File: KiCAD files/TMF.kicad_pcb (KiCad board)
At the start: 2 copper layers, 100 x 103 mm, 90 parts, among them J1 Conn_01x04_Pin, J2 Conn_01x04_Pin

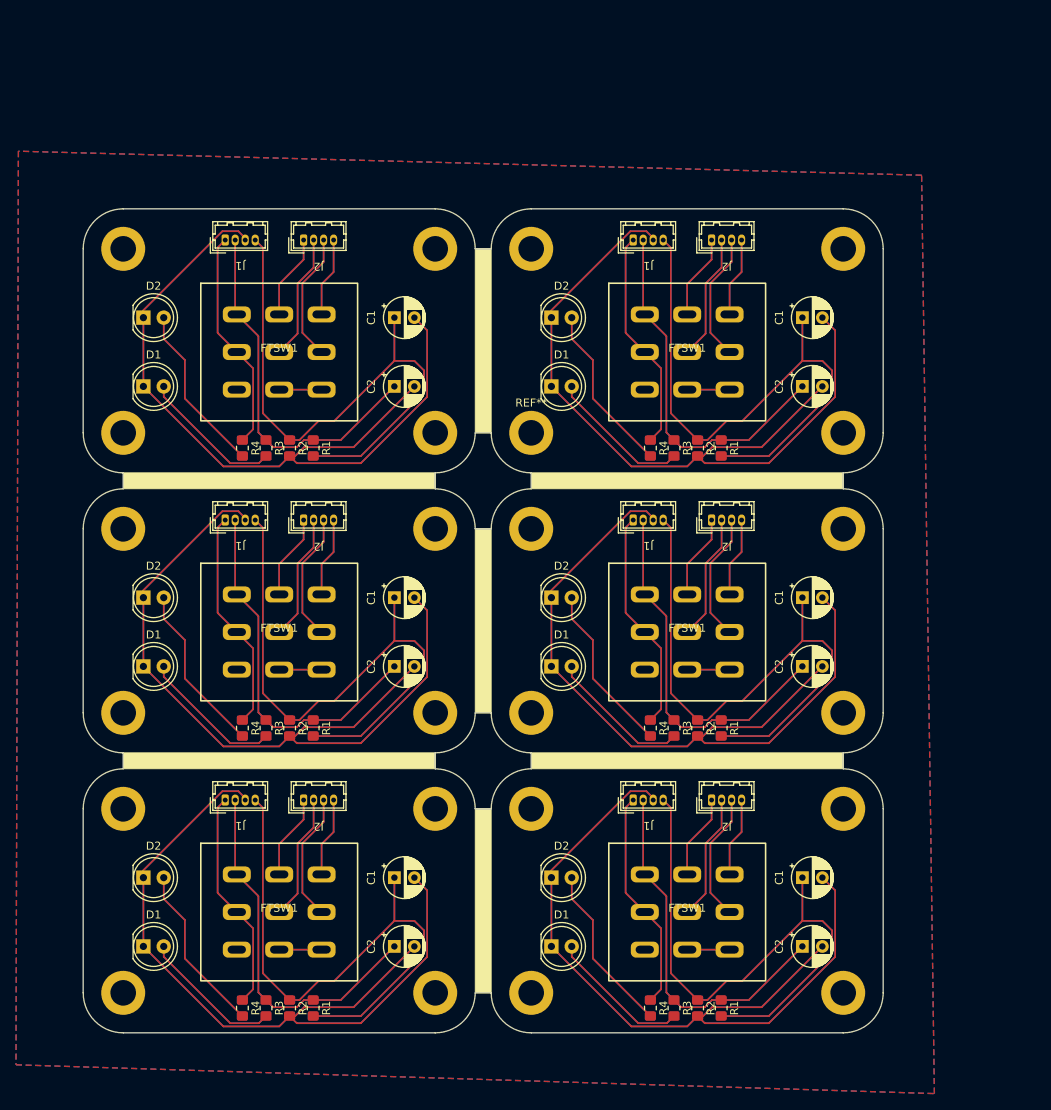
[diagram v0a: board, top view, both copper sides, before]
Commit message: Updated the gerber files
Added a ground plane and connected the screw pads to it.
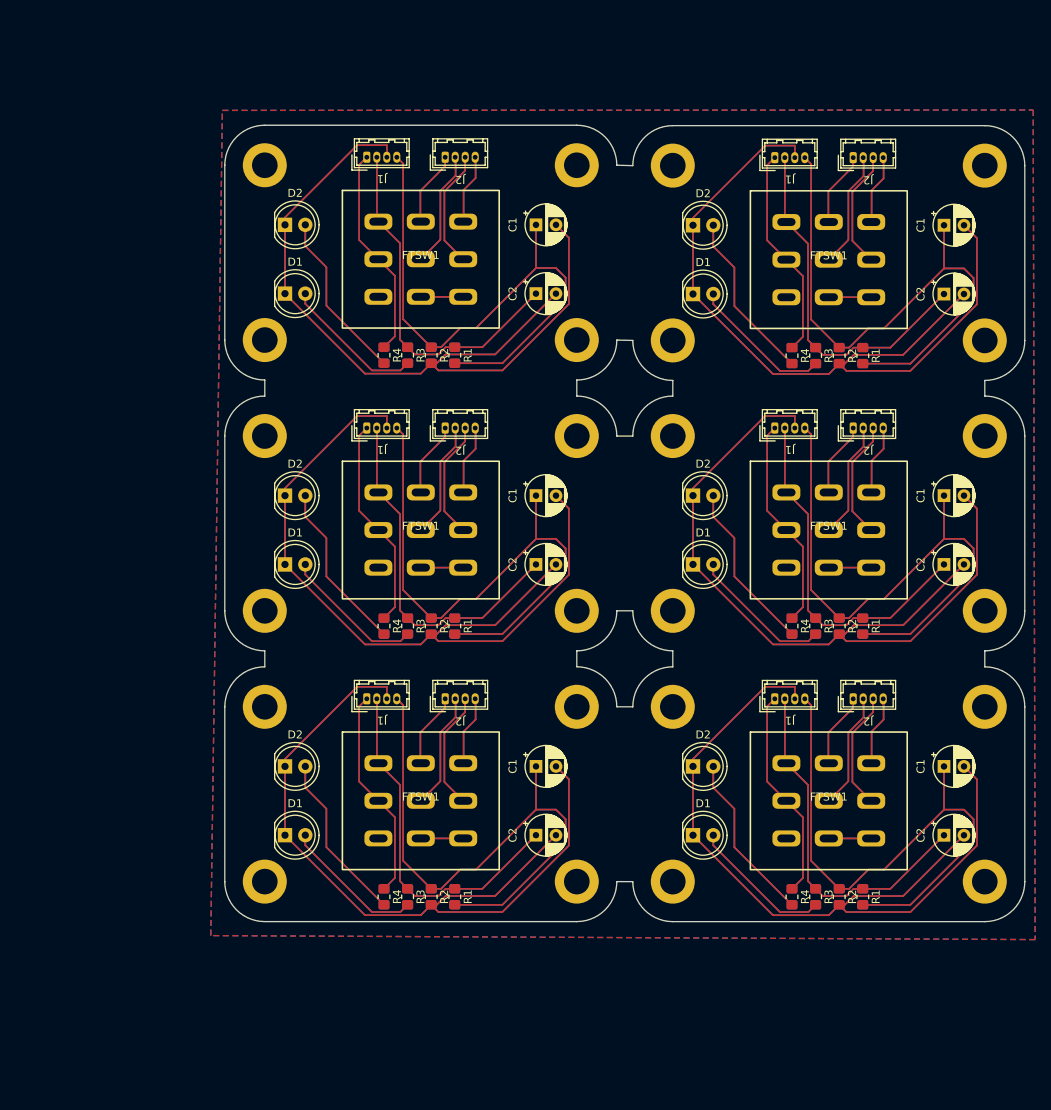
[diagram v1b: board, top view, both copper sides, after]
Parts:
- removed the ? at (188.3, 139.9)
- removed the ? at (98.3, 139.9)
- removed the ? at (188.3, 104.9)
- removed the ? at (149.3, 46.9)
- removed the ? at (137.3, 104.9)
- removed the ? at (149.3, 116.9)
- removed the ? at (188.3, 69.9)
- removed the ? at (149.3, 139.9)
- removed the ? at (149.3, 81.9)
- removed the ? at (98.3, 46.9)
- removed the ? at (98.3, 69.9)
- removed the ? at (98.3, 81.9)
- removed the ? at (98.3, 116.9)
- removed the ? at (98.3, 104.9)
- removed the ? at (137.3, 69.9)
- removed the C1 at (183.2, 55.5)
- removed the C1 at (183.2, 125.5)
- removed the C1 at (183.2, 90.5)
- removed the C1 at (132.2, 90.5)
- removed the C1 at (132.2, 125.5)
- removed the C1 at (132.2, 55.5)
- removed the C2 at (132.2, 64.1)
- removed the C2 at (132.2, 99.1)
- removed the C2 at (183.2, 99.1)
- removed the C2 at (183.2, 64.1)
- removed the C2 at (132.2, 134.1)
- removed the C2 at (183.2, 134.1)
- removed the D1 at (151.8, 134.1)
- removed the D1 at (151.8, 99.1)
- removed the D1 at (100.8, 134.1)
- removed the D1 at (100.8, 64.1)
- removed the D1 at (100.8, 99.1)
- removed the D1 at (151.8, 64.1)
- removed the D2 at (100.8, 90.5)
- removed the D2 at (151.8, 55.5)
- removed the D2 at (151.8, 90.5)
- removed the D2 at (100.8, 125.5)
- removed the D2 at (100.8, 55.5)
- removed the D2 at (151.8, 125.5)
- removed the FTSW1 at (168.8, 59.8)
- removed the FTSW1 at (168.8, 94.8)
- removed the FTSW1 at (117.8, 129.8)
- removed the FTSW1 at (117.8, 94.8)
- removed the FTSW1 at (117.8, 59.8)
- removed the FTSW1 at (168.8, 129.8)
- removed the J1 at (111.0, 80.8)
- removed the J1 at (162.1, 45.8)
- removed the J1 at (111.0, 115.8)
- removed the J1 at (162.1, 80.8)
- removed the J1 at (162.1, 115.8)
- removed the J1 at (111.0, 45.8)
- removed the J2 at (171.8, 45.8)
- removed the J2 at (171.8, 80.8)
- removed the J2 at (120.8, 45.8)
- removed the J2 at (171.8, 115.8)
- removed the J2 at (120.8, 80.8)
- removed the J2 at (120.8, 115.8)
- removed the R1 at (173.1, 71.8)
- removed the R1 at (173.1, 141.8)
- removed the R1 at (122.0, 71.8)
- removed the R1 at (122.0, 141.8)
- removed the R1 at (173.1, 106.8)
- removed the R1 at (122.0, 106.8)
- removed the R2 at (170.1, 106.8)
- removed the R2 at (170.1, 71.8)
- removed the R2 at (170.1, 141.8)
- removed the R2 at (119.1, 141.8)
- removed the R2 at (119.1, 106.8)
- removed the R2 at (119.1, 71.8)
- removed the R3 at (167.2, 106.8)
- removed the R3 at (116.2, 106.8)
- removed the R3 at (167.2, 71.8)
- removed the R3 at (116.2, 71.8)
- removed the R3 at (116.2, 141.8)
- removed the R3 at (167.2, 141.8)
- removed the R4 at (164.2, 71.8)
- removed the R4 at (113.2, 141.8)
- removed the R4 at (164.2, 141.8)
- removed the R4 at (113.2, 71.8)
- removed the R4 at (113.2, 106.8)
- removed the R4 at (164.2, 106.8)
- removed the REF** at (137.3, 139.9)
- removed the REF** at (137.3, 116.9)
- removed the REF** at (188.3, 116.9)
- removed the REF** at (137.3, 46.9)
- removed the REF** at (149.3, 69.9)
- removed the REF** at (188.3, 46.9)
- removed the REF** at (137.3, 81.9)
- removed the REF** at (149.3, 104.9)
- removed the REF** at (188.3, 81.9)
- added ?: , , F.Cu at (167.0, 126.0)
- added ?: , , F.Cu at (167.0, 92.2)
- added ?: , , F.Cu at (116.0, 58.3)
- added ?: , , F.Cu at (116.0, 104.1)
- added ?: , , F.Cu at (167.0, 104.2)
- added ?: , , F.Cu at (116.0, 70.3)
- added ?: , , F.Cu at (116.0, 92.2)
- added ?: , , F.Cu at (116.0, 126.0)
- added ?: , , F.Cu at (116.0, 36.5)
- added ?: , , F.Cu at (167.0, 58.4)
- added ?: , , F.Cu at (167.0, 70.3)
- added ?: , , F.Cu at (167.0, 36.5)
- added C1: 10µF, Capacitor_THT:CP_Radial_D5.0mm_P2.50mm, F.Cu at (149.9, 43.9)
- added C1: 10µF, Capacitor_THT:CP_Radial_D5.0mm_P2.50mm, F.Cu at (149.9, 111.6)
- added C1: 10µF, Capacitor_THT:CP_Radial_D5.0mm_P2.50mm, F.Cu at (149.9, 77.8)
- added C1: 10µF, Capacitor_THT:CP_Radial_D5.0mm_P2.50mm, F.Cu at (200.9, 111.6)
- added C1: 10µF, Capacitor_THT:CP_Radial_D5.0mm_P2.50mm, F.Cu at (200.9, 44.0)
- added C1: 10µF, Capacitor_THT:CP_Radial_D5.0mm_P2.50mm, F.Cu at (200.9, 77.8)
- added C2: 100µF, Capacitor_THT:CP_Radial_D5.0mm_P2.50mm, F.Cu at (200.9, 86.4)
- added C2: 100µF, Capacitor_THT:CP_Radial_D5.0mm_P2.50mm, F.Cu at (149.9, 120.2)
- added C2: 100µF, Capacitor_THT:CP_Radial_D5.0mm_P2.50mm, F.Cu at (149.9, 52.5)
- added C2: 100µF, Capacitor_THT:CP_Radial_D5.0mm_P2.50mm, F.Cu at (149.9, 86.4)
- added C2: 100µF, Capacitor_THT:CP_Radial_D5.0mm_P2.50mm, F.Cu at (200.9, 120.2)
- added C2: 100µF, Capacitor_THT:CP_Radial_D5.0mm_P2.50mm, F.Cu at (200.9, 52.6)
- added D1: EFFECT, LED_THT:LED_D5.0mm_Clear, F.Cu at (118.5, 86.4)
- added D1: EFFECT, LED_THT:LED_D5.0mm_Clear, F.Cu at (118.5, 52.5)
- added D1: EFFECT, LED_THT:LED_D5.0mm_Clear, F.Cu at (118.5, 120.2)
- added D1: EFFECT, LED_THT:LED_D5.0mm_Clear, F.Cu at (169.5, 120.2)
- added D1: EFFECT, LED_THT:LED_D5.0mm_Clear, F.Cu at (169.5, 86.4)
- added D1: EFFECT, LED_THT:LED_D5.0mm_Clear, F.Cu at (169.5, 52.6)
- added D2: POW, LED_THT:LED_D5.0mm_Clear, F.Cu at (118.5, 77.8)
- added D2: POW, LED_THT:LED_D5.0mm_Clear, F.Cu at (118.5, 43.9)
- added D2: POW, LED_THT:LED_D5.0mm_Clear, F.Cu at (169.5, 111.6)
- added D2: POW, LED_THT:LED_D5.0mm_Clear, F.Cu at (118.5, 111.6)
- added D2: POW, LED_THT:LED_D5.0mm_Clear, F.Cu at (169.5, 77.8)
- added D2: POW, LED_THT:LED_D5.0mm_Clear, F.Cu at (169.5, 44.0)
- added FTSW1: ~, Footswitch:3PDT Footswitch, F.Cu at (135.5, 48.2)
- added FTSW1: ~, Footswitch:3PDT Footswitch, F.Cu at (186.5, 115.9)
- added FTSW1: ~, Footswitch:3PDT Footswitch, F.Cu at (135.5, 115.9)
- added FTSW1: ~, Footswitch:3PDT Footswitch, F.Cu at (186.5, 48.3)
- added FTSW1: ~, Footswitch:3PDT Footswitch, F.Cu at (186.5, 82.1)
- added FTSW1: ~, Footswitch:3PDT Footswitch, F.Cu at (135.5, 82.1)
- added J1: Conn_01x04_Pin, Connector_Hirose:Hirose_DF13-04P-1.25DSA_1x04_P1.25mm_Vertical, F.Cu at (179.8, 35.5)
- added J1: Conn_01x04_Pin, Connector_Hirose:Hirose_DF13-04P-1.25DSA_1x04_P1.25mm_Vertical, F.Cu at (128.8, 35.5)
- added J1: Conn_01x04_Pin, Connector_Hirose:Hirose_DF13-04P-1.25DSA_1x04_P1.25mm_Vertical, F.Cu at (179.8, 103.2)
- added J1: Conn_01x04_Pin, Connector_Hirose:Hirose_DF13-04P-1.25DSA_1x04_P1.25mm_Vertical, F.Cu at (128.8, 69.3)
- added J1: Conn_01x04_Pin, Connector_Hirose:Hirose_DF13-04P-1.25DSA_1x04_P1.25mm_Vertical, F.Cu at (179.8, 69.3)
- added J1: Conn_01x04_Pin, Connector_Hirose:Hirose_DF13-04P-1.25DSA_1x04_P1.25mm_Vertical, F.Cu at (128.8, 103.2)
- added J2: Conn_01x04_Pin, Connector_Hirose:Hirose_DF13-04P-1.25DSA_1x04_P1.25mm_Vertical, F.Cu at (138.6, 35.5)
- added J2: Conn_01x04_Pin, Connector_Hirose:Hirose_DF13-04P-1.25DSA_1x04_P1.25mm_Vertical, F.Cu at (189.6, 35.5)
- added J2: Conn_01x04_Pin, Connector_Hirose:Hirose_DF13-04P-1.25DSA_1x04_P1.25mm_Vertical, F.Cu at (138.6, 69.3)
- added J2: Conn_01x04_Pin, Connector_Hirose:Hirose_DF13-04P-1.25DSA_1x04_P1.25mm_Vertical, F.Cu at (138.6, 103.2)
- added J2: Conn_01x04_Pin, Connector_Hirose:Hirose_DF13-04P-1.25DSA_1x04_P1.25mm_Vertical, F.Cu at (189.6, 103.2)
- added J2: Conn_01x04_Pin, Connector_Hirose:Hirose_DF13-04P-1.25DSA_1x04_P1.25mm_Vertical, F.Cu at (189.6, 69.3)
- added R1: 10kΩ, Resistor_SMD:R_0805_2012Metric_Pad1.20x1.40mm_HandSolder, F.Cu at (190.8, 60.3)
- added R1: 10kΩ, Resistor_SMD:R_0805_2012Metric_Pad1.20x1.40mm_HandSolder, F.Cu at (190.8, 94.1)
- added R1: 10kΩ, Resistor_SMD:R_0805_2012Metric_Pad1.20x1.40mm_HandSolder, F.Cu at (139.8, 127.9)
- added R1: 10kΩ, Resistor_SMD:R_0805_2012Metric_Pad1.20x1.40mm_HandSolder, F.Cu at (139.8, 94.1)
- added R1: 10kΩ, Resistor_SMD:R_0805_2012Metric_Pad1.20x1.40mm_HandSolder, F.Cu at (139.8, 60.2)
- added R1: 10kΩ, Resistor_SMD:R_0805_2012Metric_Pad1.20x1.40mm_HandSolder, F.Cu at (190.8, 127.9)
- added R2: 10kΩ, Resistor_SMD:R_0805_2012Metric_Pad1.20x1.40mm_HandSolder, F.Cu at (136.8, 94.1)
- added R2: 10kΩ, Resistor_SMD:R_0805_2012Metric_Pad1.20x1.40mm_HandSolder, F.Cu at (187.8, 94.1)
- added R2: 10kΩ, Resistor_SMD:R_0805_2012Metric_Pad1.20x1.40mm_HandSolder, F.Cu at (136.8, 60.2)
- added R2: 10kΩ, Resistor_SMD:R_0805_2012Metric_Pad1.20x1.40mm_HandSolder, F.Cu at (187.8, 127.9)
- added R2: 10kΩ, Resistor_SMD:R_0805_2012Metric_Pad1.20x1.40mm_HandSolder, F.Cu at (136.8, 127.9)
- added R2: 10kΩ, Resistor_SMD:R_0805_2012Metric_Pad1.20x1.40mm_HandSolder, F.Cu at (187.8, 60.3)
- added R3: 1kΩ, Resistor_SMD:R_0805_2012Metric_Pad1.20x1.40mm_HandSolder, F.Cu at (184.8, 94.1)
- added R3: 1kΩ, Resistor_SMD:R_0805_2012Metric_Pad1.20x1.40mm_HandSolder, F.Cu at (133.8, 94.1)
- added R3: 1kΩ, Resistor_SMD:R_0805_2012Metric_Pad1.20x1.40mm_HandSolder, F.Cu at (184.8, 127.9)
- added R3: 1kΩ, Resistor_SMD:R_0805_2012Metric_Pad1.20x1.40mm_HandSolder, F.Cu at (133.8, 127.9)
- added R3: 1kΩ, Resistor_SMD:R_0805_2012Metric_Pad1.20x1.40mm_HandSolder, F.Cu at (133.8, 60.2)
- added R3: 1kΩ, Resistor_SMD:R_0805_2012Metric_Pad1.20x1.40mm_HandSolder, F.Cu at (184.8, 60.3)
- added R4: 1kΩ, Resistor_SMD:R_0805_2012Metric_Pad1.20x1.40mm_HandSolder, F.Cu at (130.9, 60.2)
- added R4: 1kΩ, Resistor_SMD:R_0805_2012Metric_Pad1.20x1.40mm_HandSolder, F.Cu at (181.9, 60.3)
- added R4: 1kΩ, Resistor_SMD:R_0805_2012Metric_Pad1.20x1.40mm_HandSolder, F.Cu at (181.9, 127.9)
- added R4: 1kΩ, Resistor_SMD:R_0805_2012Metric_Pad1.20x1.40mm_HandSolder, F.Cu at (130.9, 94.1)
- added R4: 1kΩ, Resistor_SMD:R_0805_2012Metric_Pad1.20x1.40mm_HandSolder, F.Cu at (130.9, 127.9)
- added R4: 1kΩ, Resistor_SMD:R_0805_2012Metric_Pad1.20x1.40mm_HandSolder, F.Cu at (181.9, 94.1)
- added REF**: MountingHole_3.2mm_M3_ISO14580_Pad, MountingHole:MountingHole_3.2mm_M3_ISO14580_Pad, F.Cu at (206.0, 70.3)
- added REF**: MountingHole_3.2mm_M3_ISO14580_Pad, MountingHole:MountingHole_3.2mm_M3_ISO14580_Pad, F.Cu at (155.0, 104.2)
- added REF**: MountingHole_3.2mm_M3_ISO14580_Pad, MountingHole:MountingHole_3.2mm_M3_ISO14580_Pad, F.Cu at (155.0, 92.2)
- added REF**: MountingHole_3.2mm_M3_ISO14580_Pad, MountingHole:MountingHole_3.2mm_M3_ISO14580_Pad, F.Cu at (155.0, 70.3)
- added REF**: MountingHole_3.2mm_M3_ISO14580_Pad, MountingHole:MountingHole_3.2mm_M3_ISO14580_Pad, F.Cu at (155.0, 126.0)
- added REF**: MountingHole_3.2mm_M3_ISO14580_Pad, MountingHole:MountingHole_3.2mm_M3_ISO14580_Pad, F.Cu at (206.0, 104.2)
- added REF**: MountingHole_3.2mm_M3_ISO14580_Pad, MountingHole:MountingHole_3.2mm_M3_ISO14580_Pad, F.Cu at (155.0, 58.3)
- added REF**: MountingHole_3.2mm_M3_ISO14580_Pad, MountingHole:MountingHole_3.2mm_M3_ISO14580_Pad, F.Cu at (206.0, 92.2)
- added REF**: MountingHole_3.2mm_M3_ISO14580_Pad, MountingHole:MountingHole_3.2mm_M3_ISO14580_Pad, F.Cu at (206.0, 58.4)
- added REF**: MountingHole_3.2mm_M3_ISO14580_Pad, MountingHole:MountingHole_3.2mm_M3_ISO14580_Pad, F.Cu at (206.0, 36.5)
- added REF**: MountingHole_3.2mm_M3_ISO14580_Pad, MountingHole:MountingHole_3.2mm_M3_ISO14580_Pad, F.Cu at (155.0, 36.5)
- added REF**: MountingHole_3.2mm_M3_ISO14580_Pad, MountingHole:MountingHole_3.2mm_M3_ISO14580_Pad, F.Cu at (206.0, 126.0)
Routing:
- net out: track 193.1 -> 177.6 mm
- net +4,5v: track 882.0 -> 867.0 mm
- net +batt: track 333.6 -> 318.6 mm
- net +9v: track 553.9 -> 538.9 mm
- net in: track 189.4 -> 174.7 mm
- net effect_in: track 126.8 -> 112.3 mm
- net effect_out: track 119.1 -> 104.8 mm
- net GND: track 1208.0 -> 1209.0 mm
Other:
- board size 100 x 103 mm -> 100 x 99.5 mm

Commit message: Added vias
Updated the PCB. Added vias to better connect the ground planes to avoid unwanted capacitance between the planes
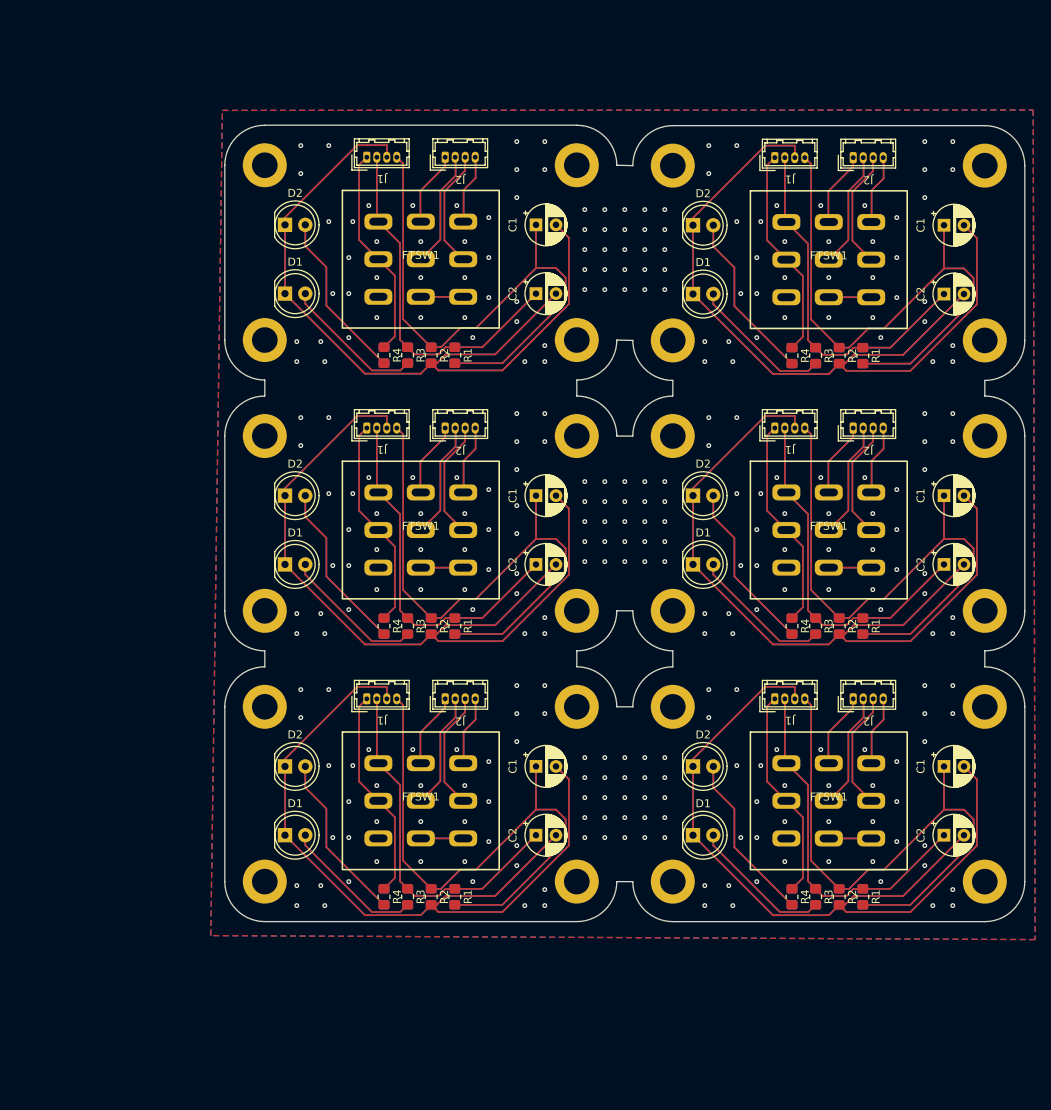
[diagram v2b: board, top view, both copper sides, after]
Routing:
- net GND: vias 0 -> 311

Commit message: Redone PCB
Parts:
- removed the ? at (167.0, 126.0)
- removed the ? at (167.0, 92.2)
- removed the ? at (116.0, 58.3)
- removed the ? at (167.0, 104.2)
- removed the ? at (116.0, 70.3)
- removed the ? at (116.0, 92.2)
- removed the ? at (116.0, 36.5)
- removed the ? at (167.0, 58.4)
- removed the ? at (167.0, 70.3)
- removed the ? at (167.0, 36.5)
- removed the C1 at (149.9, 43.9)
- removed the C1 at (149.9, 111.6)
- removed the C1 at (149.9, 77.8)
- removed the C1 at (200.9, 111.6)
- removed the C1 at (200.9, 44.0)
- removed the C1 at (200.9, 77.8)
- removed the C2 at (200.9, 86.4)
- removed the C2 at (149.9, 120.2)
- removed the C2 at (149.9, 52.5)
- removed the C2 at (149.9, 86.4)
- removed the C2 at (200.9, 120.2)
- removed the C2 at (200.9, 52.6)
- removed the D1 at (118.5, 86.4)
- removed the D1 at (118.5, 52.5)
- removed the D1 at (118.5, 120.2)
- removed the D1 at (169.5, 120.2)
- removed the D1 at (169.5, 86.4)
- removed the D1 at (169.5, 52.6)
- removed the D2 at (118.5, 77.8)
- removed the D2 at (118.5, 43.9)
- removed the D2 at (169.5, 111.6)
- removed the D2 at (118.5, 111.6)
- removed the D2 at (169.5, 77.8)
- removed the D2 at (169.5, 44.0)
- removed the FTSW1 at (135.5, 48.2)
- removed the FTSW1 at (186.5, 115.9)
- removed the FTSW1 at (135.5, 115.9)
- removed the FTSW1 at (186.5, 48.3)
- removed the FTSW1 at (186.5, 82.1)
- removed the FTSW1 at (135.5, 82.1)
- removed the J1 at (179.8, 35.5)
- removed the J1 at (128.8, 35.5)
- removed the J1 at (179.8, 103.2)
- removed the J1 at (128.8, 69.3)
- removed the J1 at (179.8, 69.3)
- removed the J1 at (128.8, 103.2)
- removed the J2 at (138.6, 35.5)
- removed the J2 at (189.6, 35.5)
- removed the J2 at (138.6, 69.3)
- removed the J2 at (138.6, 103.2)
- removed the J2 at (189.6, 103.2)
- removed the J2 at (189.6, 69.3)
- removed the R1 at (190.8, 60.3)
- removed the R1 at (190.8, 94.1)
- removed the R1 at (139.8, 127.9)
- removed the R1 at (139.8, 94.1)
- removed the R1 at (139.8, 60.2)
- removed the R1 at (190.8, 127.9)
- removed the R2 at (136.8, 94.1)
- removed the R2 at (187.8, 94.1)
- removed the R2 at (136.8, 60.2)
- removed the R2 at (187.8, 127.9)
- removed the R2 at (136.8, 127.9)
- removed the R2 at (187.8, 60.3)
- removed the R3 at (184.8, 94.1)
- removed the R3 at (133.8, 94.1)
- removed the R3 at (184.8, 127.9)
- removed the R3 at (133.8, 127.9)
- removed the R3 at (133.8, 60.2)
- removed the R3 at (184.8, 60.3)
- removed the R4 at (130.9, 60.2)
- removed the R4 at (181.9, 60.3)
- removed the R4 at (181.9, 127.9)
- removed the R4 at (130.9, 94.1)
- removed the R4 at (130.9, 127.9)
- removed the R4 at (181.9, 94.1)
- removed the REF** at (206.0, 70.3)
- removed the REF** at (155.0, 92.2)
- removed the REF** at (155.0, 70.3)
- removed the REF** at (206.0, 104.2)
- removed the REF** at (155.0, 58.3)
- removed the REF** at (206.0, 92.2)
- removed the REF** at (206.0, 58.4)
- removed the REF** at (206.0, 36.5)
- removed the REF** at (155.0, 36.5)
- removed the REF** at (206.0, 126.0)
- added +4.5v: TestPoint_Pad_D2.0mm, TestPoint:TestPoint_Pad_D2.0mm, F.Cu at (183.0, 117.4)
- added +4.5v: TestPoint_Pad_D2.0mm, TestPoint:TestPoint_Pad_D2.0mm, F.Cu at (132.9, 51.7)
- added +4.5v: TestPoint_Pad_D2.0mm, TestPoint:TestPoint_Pad_D2.0mm, F.Cu at (183.0, 51.6)
- added +4.5v: TestPoint_Pad_D2.0mm, TestPoint:TestPoint_Pad_D2.0mm, F.Cu at (183.0, 84.5)
- added +4.5v: TestPoint_Pad_D2.0mm, TestPoint:TestPoint_Pad_D2.0mm, F.Cu at (132.9, 84.5)
- added +4.5v: TestPoint_Pad_D2.0mm, TestPoint:TestPoint_Pad_D2.0mm, F.Cu at (133.1, 117.4)
- added ?: , , F.Cu at (112.9, 82.1)
- added ?: , , F.Cu at (112.9, 27.4)
- added ?: , , F.Cu at (112.9, 49.3)
- added ?: , , F.Cu at (163.0, 49.2)
- added ?: , , F.Cu at (163.0, 27.3)
- added ?: , , F.Cu at (163.0, 93.1)
- added ?: , , F.Cu at (163.0, 115.0)
- added ?: , , F.Cu at (112.9, 60.2)
- added ?: , , F.Cu at (163.0, 60.2)
- added ?: , , F.Cu at (163.0, 82.1)
- added C1: 10µF, Capacitor_THT:CP_Radial_D5.0mm_P2.50mm, F.Cu at (197.1, 40.1)
- added C1: 10µF, Capacitor_THT:CP_Radial_D5.0mm_P2.50mm, F.Cu at (147.0, 73.0)
- added C1: 10µF, Capacitor_THT:CP_Radial_D5.0mm_P2.50mm, F.Cu at (147.0, 40.2)
- added C1: 10µF, Capacitor_THT:CP_Radial_D5.0mm_P2.50mm, F.Cu at (147.2, 105.9)
- added C1: 10µF, Capacitor_THT:CP_Radial_D5.0mm_P2.50mm, F.Cu at (197.1, 105.9)
- added C1: 10µF, Capacitor_THT:CP_Radial_D5.0mm_P2.50mm, F.Cu at (197.1, 73.0)
- added C2: 100µF, Capacitor_THT:CP_Radial_D5.0mm_P2.50mm, F.Cu at (194.7, 34.3)
- added C2: 100µF, Capacitor_THT:CP_Radial_D5.0mm_P2.50mm, F.Cu at (194.7, 67.2)
- added C2: 100µF, Capacitor_THT:CP_Radial_D5.0mm_P2.50mm, F.Cu at (144.8, 100.1)
- added C2: 100µF, Capacitor_THT:CP_Radial_D5.0mm_P2.50mm, F.Cu at (194.7, 100.1)
- added C2: 100µF, Capacitor_THT:CP_Radial_D5.0mm_P2.50mm, F.Cu at (144.6, 34.4)
- added C2: 100µF, Capacitor_THT:CP_Radial_D5.0mm_P2.50mm, F.Cu at (144.6, 67.2)
- added D1: EFFECT, LED_THT:LED_D5.0mm_Clear, F.Cu at (124.6, 58.9)
- added D1: EFFECT, LED_THT:LED_D5.0mm_Clear, F.Cu at (174.7, 58.9)
- added D1: EFFECT, LED_THT:LED_D5.0mm_Clear, F.Cu at (124.8, 91.8)
- added D1: EFFECT, LED_THT:LED_D5.0mm_Clear, F.Cu at (174.7, 91.8)
- added D1: EFFECT, LED_THT:LED_D5.0mm_Clear, F.Cu at (124.6, 26.1)
- added D1: EFFECT, LED_THT:LED_D5.0mm_Clear, F.Cu at (174.7, 26.0)
- added D2: POW, LED_THT:LED_D5.0mm_Clear, F.Cu at (137.9, 91.8)
- added D2: POW, LED_THT:LED_D5.0mm_Clear, F.Cu at (137.7, 58.9)
- added D2: POW, LED_THT:LED_D5.0mm_Clear, F.Cu at (187.8, 58.9)
- added D2: POW, LED_THT:LED_D5.0mm_Clear, F.Cu at (187.8, 91.8)
- added D2: POW, LED_THT:LED_D5.0mm_Clear, F.Cu at (187.8, 26.0)
- added D2: POW, LED_THT:LED_D5.0mm_Clear, F.Cu at (137.7, 26.1)
- added FTSW1: ~, Footswitch:3PDT Footswitch, F.Cu at (132.6, 104.1)
- added FTSW1: ~, Footswitch:3PDT Footswitch, F.Cu at (182.5, 38.3)
- added FTSW1: ~, Footswitch:3PDT Footswitch, F.Cu at (182.5, 104.1)
- added FTSW1: ~, Footswitch:3PDT Footswitch, F.Cu at (132.4, 38.4)
- added FTSW1: ~, Footswitch:3PDT Footswitch, F.Cu at (182.5, 71.2)
- added FTSW1: ~, Footswitch:3PDT Footswitch, F.Cu at (132.4, 71.2)
- added In: TestPoint_Pad_D2.0mm, TestPoint:TestPoint_Pad_D2.0mm, F.Cu at (204.1, 34.7)
- added In: TestPoint_Pad_D2.0mm, TestPoint:TestPoint_Pad_D2.0mm, F.Cu at (154.0, 67.6)
- added In: TestPoint_Pad_D2.0mm, TestPoint:TestPoint_Pad_D2.0mm, F.Cu at (154.2, 100.5)
- added In: TestPoint_Pad_D2.0mm, TestPoint:TestPoint_Pad_D2.0mm, F.Cu at (204.1, 100.5)
- added In: TestPoint_Pad_D2.0mm, TestPoint:TestPoint_Pad_D2.0mm, F.Cu at (204.1, 67.6)
- added In: TestPoint_Pad_D2.0mm, TestPoint:TestPoint_Pad_D2.0mm, F.Cu at (154.0, 34.8)
- added J1: DST-2, Connector_JST:JST_XH_B4B-XH-A_1x04_P2.50mm_Vertical, F.Cu at (126.3, 51.4)
- added J1: DST-2, Connector_JST:JST_XH_B4B-XH-A_1x04_P2.50mm_Vertical, F.Cu at (176.4, 117.1)
- added J1: DST-2, Connector_JST:JST_XH_B4B-XH-A_1x04_P2.50mm_Vertical, F.Cu at (126.5, 117.1)
- added J1: DST-2, Connector_JST:JST_XH_B4B-XH-A_1x04_P2.50mm_Vertical, F.Cu at (176.4, 51.3)
- added J1: DST-2, Connector_JST:JST_XH_B4B-XH-A_1x04_P2.50mm_Vertical, F.Cu at (126.3, 84.2)
- added J1: DST-2, Connector_JST:JST_XH_B4B-XH-A_1x04_P2.50mm_Vertical, F.Cu at (176.4, 84.2)
- added J2: TMC-1, Connector_JST:JST_XH_B2B-XH-A_1x02_P2.50mm_Vertical, F.Cu at (154.2, 106.5)
- added J2: TMC-1, Connector_JST:JST_XH_B2B-XH-A_1x02_P2.50mm_Vertical, F.Cu at (204.1, 106.5)
- added J2: TMC-1, Connector_JST:JST_XH_B2B-XH-A_1x02_P2.50mm_Vertical, F.Cu at (204.1, 40.7)
- added J2: TMC-1, Connector_JST:JST_XH_B2B-XH-A_1x02_P2.50mm_Vertical, F.Cu at (154.0, 73.6)
- added J2: TMC-1, Connector_JST:JST_XH_B2B-XH-A_1x02_P2.50mm_Vertical, F.Cu at (204.1, 73.6)
- added J2: TMC-1, Connector_JST:JST_XH_B2B-XH-A_1x02_P2.50mm_Vertical, F.Cu at (154.0, 40.8)
- added J3: TMC-1, Connector_JST:JST_XH_B2B-XH-A_1x02_P2.50mm_Vertical, F.Cu at (160.9, 43.2)
- added J3: TMC-1, Connector_JST:JST_XH_B2B-XH-A_1x02_P2.50mm_Vertical, F.Cu at (160.9, 76.1)
- added J3: TMC-1, Connector_JST:JST_XH_B2B-XH-A_1x02_P2.50mm_Vertical, F.Cu at (160.9, 109.0)
- added J3: TMC-1, Connector_JST:JST_XH_B2B-XH-A_1x02_P2.50mm_Vertical, F.Cu at (110.8, 43.3)
- added J3: TMC-1, Connector_JST:JST_XH_B2B-XH-A_1x02_P2.50mm_Vertical, F.Cu at (111.0, 109.0)
- added J3: TMC-1, Connector_JST:JST_XH_B2B-XH-A_1x02_P2.50mm_Vertical, F.Cu at (110.8, 76.1)
- added J4: DST-2, Connector_JST:JST_XH_B2B-XH-A_1x02_P2.50mm_Vertical, F.Cu at (145.9, 51.4)
- added J4: DST-2, Connector_JST:JST_XH_B2B-XH-A_1x02_P2.50mm_Vertical, F.Cu at (196.0, 84.2)
- added J4: DST-2, Connector_JST:JST_XH_B2B-XH-A_1x02_P2.50mm_Vertical, F.Cu at (196.0, 117.1)
- added J4: DST-2, Connector_JST:JST_XH_B2B-XH-A_1x02_P2.50mm_Vertical, F.Cu at (145.9, 84.2)
- added J4: DST-2, Connector_JST:JST_XH_B2B-XH-A_1x02_P2.50mm_Vertical, F.Cu at (196.0, 51.3)
- added J4: DST-2, Connector_JST:JST_XH_B2B-XH-A_1x02_P2.50mm_Vertical, F.Cu at (146.1, 117.1)
- added Out: TestPoint_Pad_D2.0mm, TestPoint:TestPoint_Pad_D2.0mm, F.Cu at (167.3, 36.8)
- added Out: TestPoint_Pad_D2.0mm, TestPoint:TestPoint_Pad_D2.0mm, F.Cu at (117.4, 102.6)
- added Out: TestPoint_Pad_D2.0mm, TestPoint:TestPoint_Pad_D2.0mm, F.Cu at (117.2, 36.9)
- added Out: TestPoint_Pad_D2.0mm, TestPoint:TestPoint_Pad_D2.0mm, F.Cu at (117.2, 69.7)
- added Out: TestPoint_Pad_D2.0mm, TestPoint:TestPoint_Pad_D2.0mm, F.Cu at (167.3, 69.7)
- added Out: TestPoint_Pad_D2.0mm, TestPoint:TestPoint_Pad_D2.0mm, F.Cu at (167.3, 102.6)
- added R1: 10kΩ, Resistor_SMD:R_0805_2012Metric_Pad1.20x1.40mm_HandSolder, F.Cu at (194.8, 77.0)
- added R1: 10kΩ, Resistor_SMD:R_0805_2012Metric_Pad1.20x1.40mm_HandSolder, F.Cu at (144.9, 109.9)
- added R1: 10kΩ, Resistor_SMD:R_0805_2012Metric_Pad1.20x1.40mm_HandSolder, F.Cu at (194.8, 109.9)
- added R1: 10kΩ, Resistor_SMD:R_0805_2012Metric_Pad1.20x1.40mm_HandSolder, F.Cu at (144.7, 44.2)
- added R1: 10kΩ, Resistor_SMD:R_0805_2012Metric_Pad1.20x1.40mm_HandSolder, F.Cu at (144.7, 77.0)
- added R1: 10kΩ, Resistor_SMD:R_0805_2012Metric_Pad1.20x1.40mm_HandSolder, F.Cu at (194.8, 44.1)
- added R2: 10kΩ, Resistor_SMD:R_0805_2012Metric_Pad1.20x1.40mm_HandSolder, F.Cu at (194.8, 46.2)
- added R2: 10kΩ, Resistor_SMD:R_0805_2012Metric_Pad1.20x1.40mm_HandSolder, F.Cu at (144.7, 46.3)
- added R2: 10kΩ, Resistor_SMD:R_0805_2012Metric_Pad1.20x1.40mm_HandSolder, F.Cu at (194.8, 112.0)
- added R2: 10kΩ, Resistor_SMD:R_0805_2012Metric_Pad1.20x1.40mm_HandSolder, F.Cu at (194.8, 79.1)
- added R2: 10kΩ, Resistor_SMD:R_0805_2012Metric_Pad1.20x1.40mm_HandSolder, F.Cu at (144.7, 79.1)
- added R2: 10kΩ, Resistor_SMD:R_0805_2012Metric_Pad1.20x1.40mm_HandSolder, F.Cu at (144.9, 112.0)
- added R3: 1kΩ, Resistor_SMD:R_0805_2012Metric_Pad1.20x1.40mm_HandSolder, F.Cu at (171.5, 26.0)
- added R3: 1kΩ, Resistor_SMD:R_0805_2012Metric_Pad1.20x1.40mm_HandSolder, F.Cu at (171.5, 58.9)
- added R3: 1kΩ, Resistor_SMD:R_0805_2012Metric_Pad1.20x1.40mm_HandSolder, F.Cu at (121.6, 91.8)
- added R3: 1kΩ, Resistor_SMD:R_0805_2012Metric_Pad1.20x1.40mm_HandSolder, F.Cu at (121.4, 58.9)
- added R3: 1kΩ, Resistor_SMD:R_0805_2012Metric_Pad1.20x1.40mm_HandSolder, F.Cu at (171.5, 91.8)
- added R3: 1kΩ, Resistor_SMD:R_0805_2012Metric_Pad1.20x1.40mm_HandSolder, F.Cu at (121.4, 26.1)
- added R4: 1kΩ, Resistor_SMD:R_0805_2012Metric_Pad1.20x1.40mm_HandSolder, F.Cu at (193.6, 58.9)
- added R4: 1kΩ, Resistor_SMD:R_0805_2012Metric_Pad1.20x1.40mm_HandSolder, F.Cu at (193.6, 91.8)
- added R4: 1kΩ, Resistor_SMD:R_0805_2012Metric_Pad1.20x1.40mm_HandSolder, F.Cu at (143.5, 26.1)
- added R4: 1kΩ, Resistor_SMD:R_0805_2012Metric_Pad1.20x1.40mm_HandSolder, F.Cu at (143.5, 58.9)
- added R4: 1kΩ, Resistor_SMD:R_0805_2012Metric_Pad1.20x1.40mm_HandSolder, F.Cu at (143.7, 91.8)
- added R4: 1kΩ, Resistor_SMD:R_0805_2012Metric_Pad1.20x1.40mm_HandSolder, F.Cu at (193.6, 26.0)
- added REF**: MountingHole_3.2mm_M3_ISO14580_Pad, MountingHole:MountingHole_3.2mm_M3_ISO14580_Pad, F.Cu at (202.0, 115.0)
- added REF**: MountingHole_3.2mm_M3_ISO14580_Pad, MountingHole:MountingHole_3.2mm_M3_ISO14580_Pad, F.Cu at (202.0, 27.4)
- added REF**: MountingHole_3.2mm_M3_ISO14580_Pad, MountingHole:MountingHole_3.2mm_M3_ISO14580_Pad, F.Cu at (151.9, 82.1)
- added REF**: MountingHole_3.2mm_M3_ISO14580_Pad, MountingHole:MountingHole_3.2mm_M3_ISO14580_Pad, F.Cu at (151.9, 49.3)
- added REF**: MountingHole_3.2mm_M3_ISO14580_Pad, MountingHole:MountingHole_3.2mm_M3_ISO14580_Pad, F.Cu at (202.0, 82.1)
- added REF**: MountingHole_3.2mm_M3_ISO14580_Pad, MountingHole:MountingHole_3.2mm_M3_ISO14580_Pad, F.Cu at (202.0, 93.2)
- added REF**: MountingHole_3.2mm_M3_ISO14580_Pad, MountingHole:MountingHole_3.2mm_M3_ISO14580_Pad, F.Cu at (151.9, 60.3)
- added REF**: MountingHole_3.2mm_M3_ISO14580_Pad, MountingHole:MountingHole_3.2mm_M3_ISO14580_Pad, F.Cu at (202.0, 49.2)
- added REF**: MountingHole_3.2mm_M3_ISO14580_Pad, MountingHole:MountingHole_3.2mm_M3_ISO14580_Pad, F.Cu at (151.9, 27.4)
- added REF**: MountingHole_3.2mm_M3_ISO14580_Pad, MountingHole:MountingHole_3.2mm_M3_ISO14580_Pad, F.Cu at (202.0, 60.3)
- moved ? 11.4 mm to (113.1, 93.1)
- moved ? 11.4 mm to (113.1, 115.0)
- moved REF** 11.4 mm to (152.1, 93.2)
- moved REF** 11.4 mm to (152.1, 115.0)
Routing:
- net GND: track 1209.0 -> 77.3 mm, vias 311 -> 6
- net +4,5v: track 867.0 -> 174.6 mm, vias 0 -> 12
- net Net-(D2-A): track 256.5 -> 21.9 mm
- net +9v: track 538.9 -> 346.1 mm
- net Net-(D1-A): track 214.6 -> 38.8 mm
- net effect_out: track 104.8 -> 215.9 mm
- net effect_in: track 112.3 -> 183.3 mm
- net in: track 174.7 -> 228.7 mm
- net +batt: track 318.6 -> 282.7 mm, vias 0 -> 6
- net clean: track 63.6 -> 31.8 mm
- net out: track 177.6 -> 174.5 mm
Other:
- board size 100 x 99.5 mm -> 99.1 x 97.7 mm
